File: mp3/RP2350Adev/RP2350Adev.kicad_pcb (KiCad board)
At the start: 2 copper layers, 30 x 52 mm, 48 parts, among them J1 USB4105-GF-A, J2 LEFT, J4 RIGHT, U1 W25Q32JV, U2 RP2350A, U3 MCP1702T-3302E_CB, X1 IQXO-791

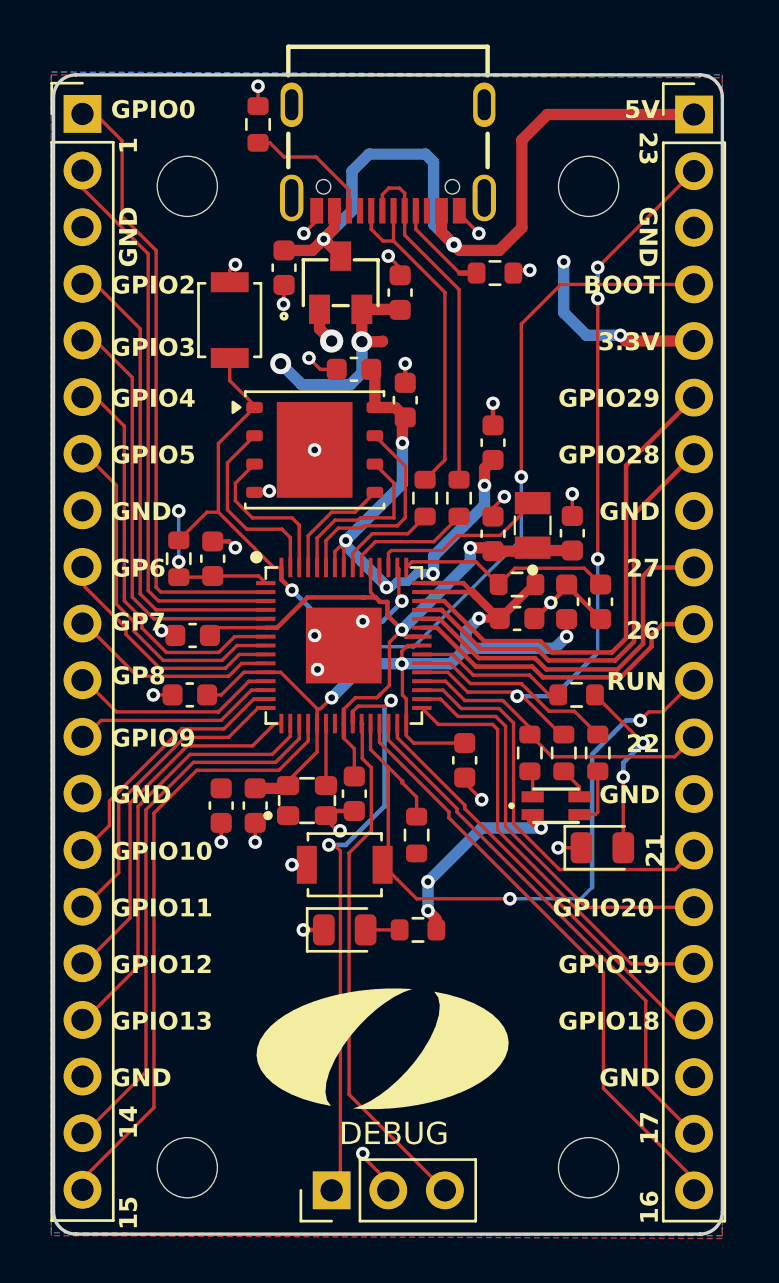
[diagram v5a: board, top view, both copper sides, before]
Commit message: Relocate flash and buck components
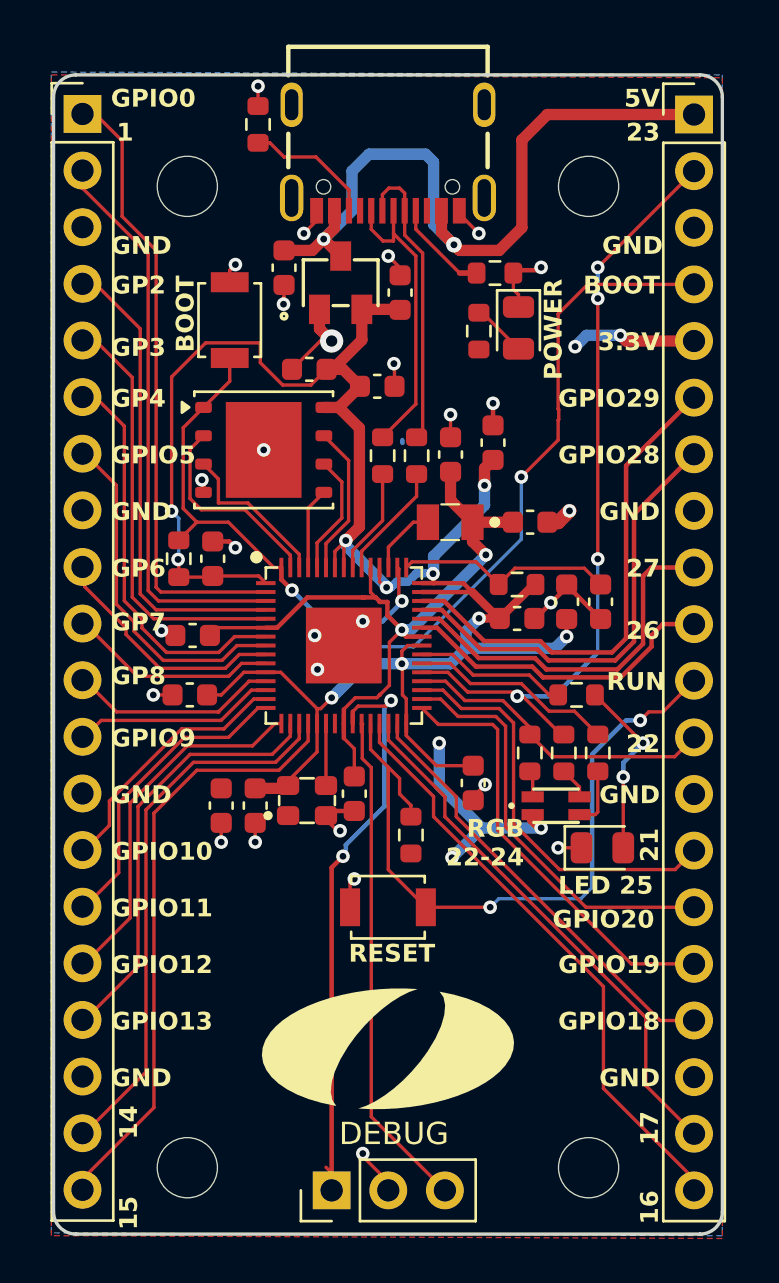
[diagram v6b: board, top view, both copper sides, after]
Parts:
- moved D3 28.1 mm to (48.5, 34.2), turned to -90 degrees
- moved R12 27.0 mm to (46.7, 34.4), turned to 90 degrees
- moved C3 4.03 mm to (45.5, 39.9)
- moved L1 3.70 mm to (45.5, 42.9), turned to 180 degrees
- moved S1 2.72 mm to (42.7, 60.2)
- moved R5 2.69 mm to (43.9, 39.9)
- moved R6 2.69 mm to (42.4, 39.9)
- moved U1 2.29 mm to (37.1, 39.7)
- moved C1 2.01 mm to (39.1, 36.1)
- moved C15 1.96 mm to (49.0, 42.9), turned to 180 degrees
- moved C10 1.40 mm to (42.2, 36.8), turned to 180 degrees
- moved C7 1.09 mm to (46.5, 54.6)
- moved R1 0.25 mm to (43.7, 57.0)
- moved OlinLogoLg 0.24 mm to (42.7, 66.5)
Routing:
- net +3V3: track 104.3 -> 114.6 mm, vias 18 -> 15
- net Net-(U2-VREG_LX): track 8.04 -> 3.15 mm
- net GND: track 44.8 -> 47.6 mm, vias 31 -> 29
- net Net-(U1-~{HOLD}/IO3): track 9.43 -> 6.79 mm
- net Net-(U1-SCK): track 7.91 -> 5.43 mm
- net Net-(J1-D--PadA7): track 15.8 -> 13.3 mm
- net Net-(J1-D+-PadA6): track 15.4 -> 13.6 mm
- net Net-(U1-DI/IO0): track 5.22 -> 3.66 mm
- net +1V1: track 31.4 -> 32.6 mm
- net Net-(D3-A): track 1.52 -> 2.45 mm
- net /SWDIO: track 23.3 -> 22.5 mm
- net Net-(U1-DO/IO1): track 8.51 -> 9.17 mm
- net /BOOT: track 47.1 -> 46.5 mm
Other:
- board text added: "GP2"
- board text added: "GP3"
- board text added: "GP4"
- board text added: "LED 25"
- board text added: "M2.5"
- board text added: "POWER"
- board text added: "RESET"
- board text added: "RGB 22-24"
- board text removed: "GPIO2"
- board text removed: "GPIO3"
- board text removed: "GPIO4"
